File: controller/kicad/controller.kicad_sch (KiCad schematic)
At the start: 22 parts, among them J1 pcie_98, U1 ESD5344D, U10 ESD5344D, U11 WeAct_STM32H750_Module, U12 ESD5344D, U13 ESD5344D, U14 ESD5344D, U15 ESD5344D, U16 ESD5344D, U17 ESD5344D, U18 ESD5344D, U19 ESD5344D, U2 ESD5344D, U20 ESD5344D, U21 ESD5344D, U3 ESD5344D, U4 ESD5344D, U5 ESD5344D, U6 ESD5344D, U7 ESD5344D, U8 ESD5344D, U9 ESD5344D

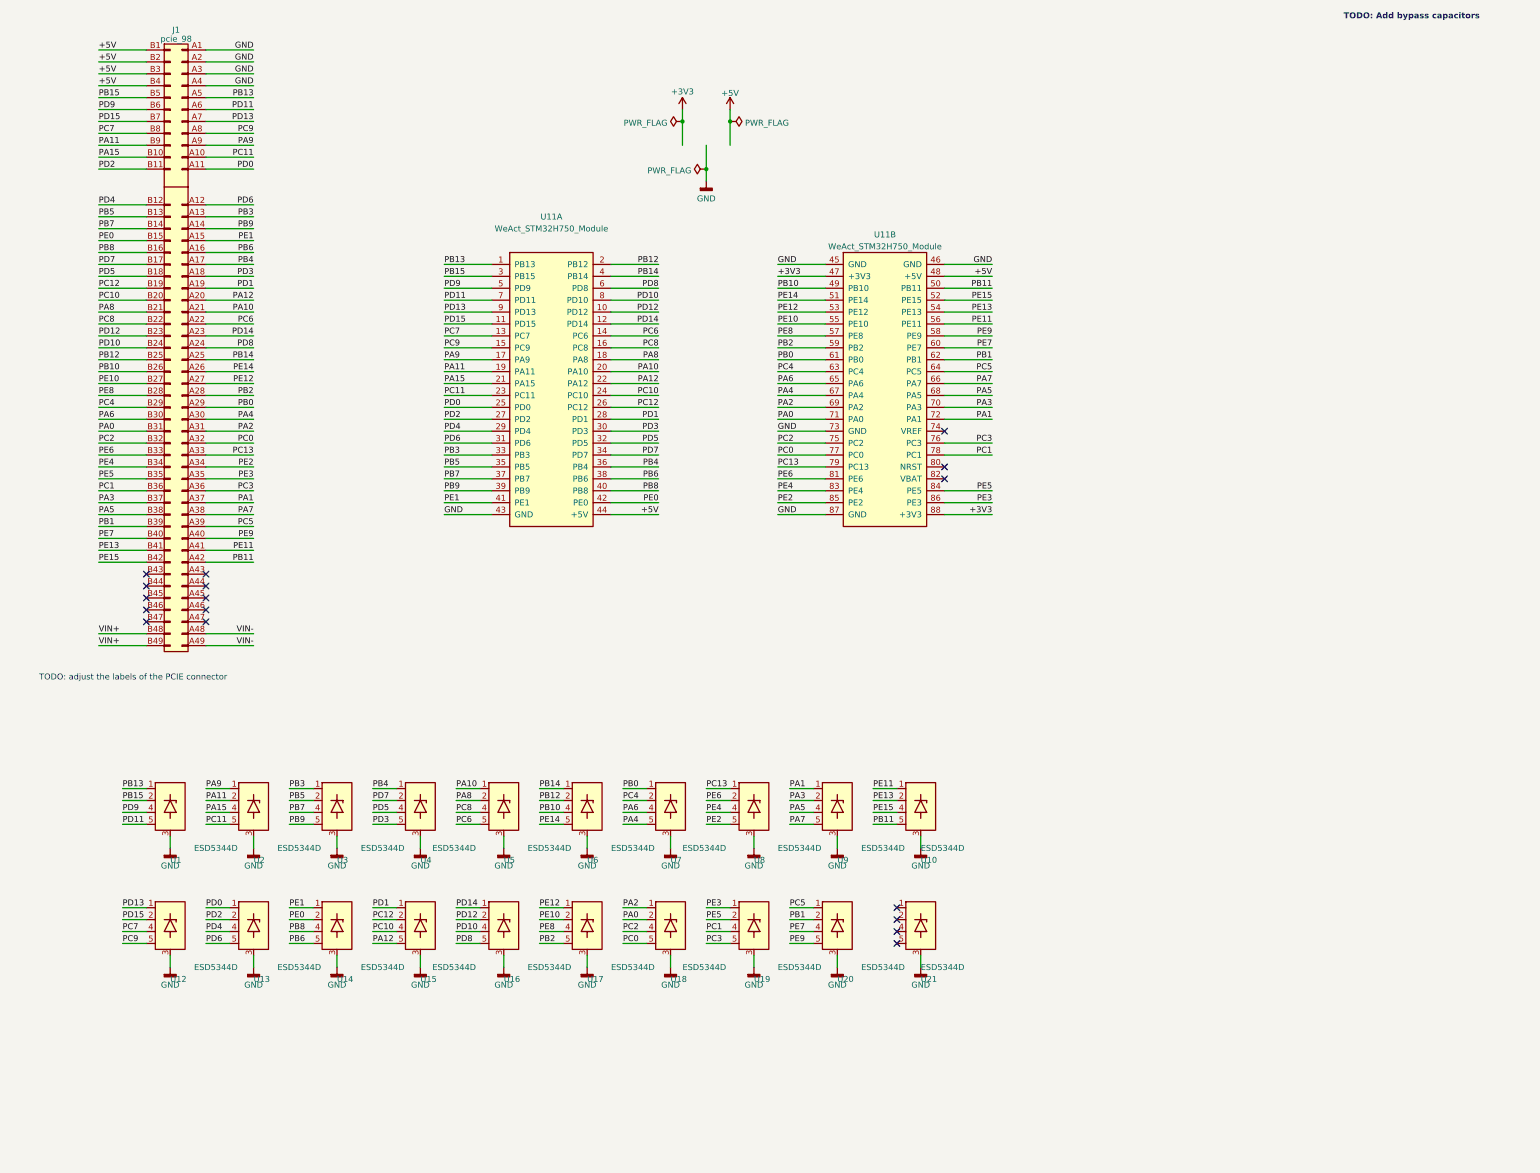
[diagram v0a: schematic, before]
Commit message: Controller board passes ERC and DRC. Needs more cleanup.
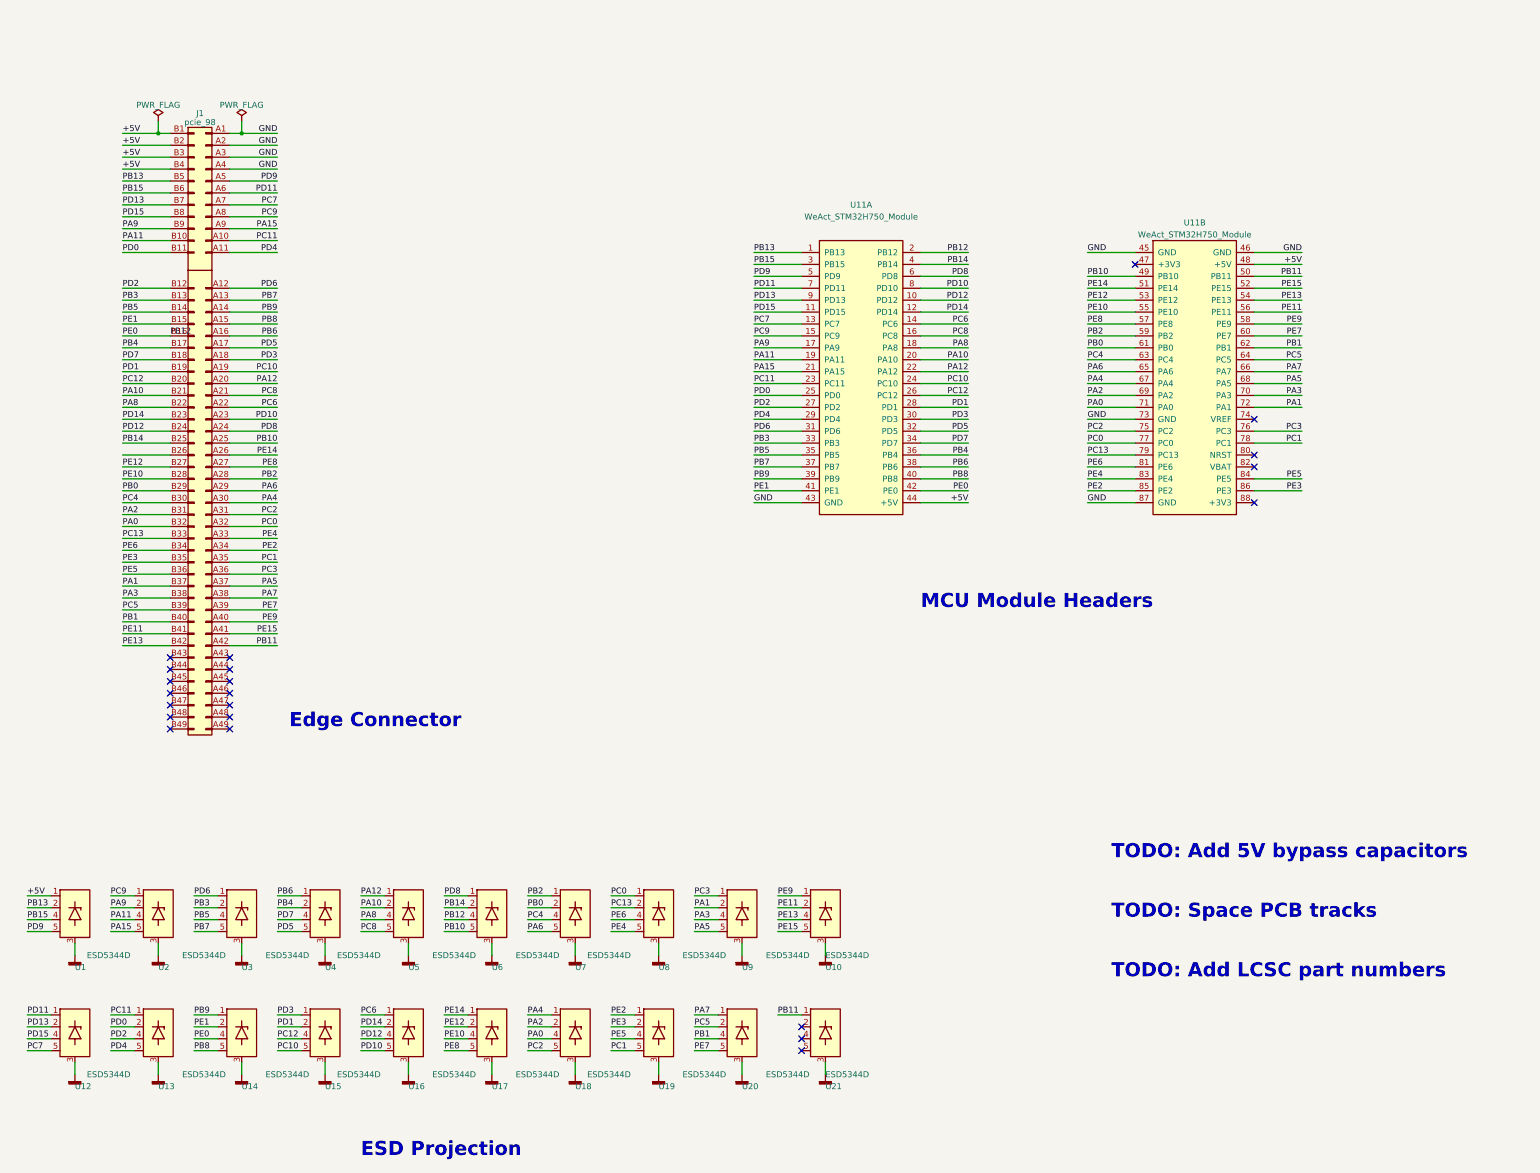
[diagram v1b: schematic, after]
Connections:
- net +5V: now also U1.1 (D1)
- net PA0: now also J1.B32 (Pin_b32), U18.4 (D3); no longer J1.B31 (Pin_b31), U18.2 (D2)
- net PA1: now also J1.B37 (Pin_b37), U9.2 (D2); no longer J1.A37 (Pin_a37), U9.1 (D1)
- net PA10: now also J1.B21 (Pin_b21), U5.2 (D2); no longer J1.A21 (Pin_a21), U5.1 (D1)
- net PA11: now also J1.B10 (Pin_b10), U2.4 (D3); no longer J1.B9 (Pin_b9), U2.2 (D2)
- net PA12: now also U5.1 (D1); no longer U15.5 (D4)
- net PA15: now also J1.A9 (Pin_a9), U2.5 (D4); no longer J1.B10 (Pin_b10), U2.4 (D3)
- net PA2: now also J1.B31 (Pin_b31), U18.2 (D2); no longer J1.A31 (Pin_a31), U18.1 (D1)
- net PA3: now also J1.B38 (Pin_b38), U9.4 (D3); no longer J1.B37 (Pin_b37), U9.2 (D2)
- net PA4: now also U18.1 (D1); no longer U7.5 (D4)
- net PA5: now also J1.A37 (Pin_a37), U9.5 (D4); no longer J1.B38 (Pin_b38), U9.4 (D3)
- net PA6: now also J1.A29 (Pin_a29), U7.5 (D4); no longer J1.B30 (Pin_b30), U7.4 (D3)
- net PA7: now also U20.1 (D1); no longer U9.5 (D4)
- net PA8: now also J1.B22 (Pin_b22), U5.4 (D3); no longer J1.B21 (Pin_b21), U5.2 (D2)
- net PA9: now also J1.B9 (Pin_b9), U2.2 (D2); no longer J1.A9 (Pin_a9), U2.1 (D1)
- net PB0: now also J1.B29 (Pin_b29), U7.2 (D2); no longer J1.A29 (Pin_a29), U7.1 (D1)
- net PB1: now also J1.B40 (Pin_b40), U20.4 (D3); no longer J1.B39 (Pin_b39), U20.2 (D2)
- net PB10: now also J1.A25 (Pin_a25), U6.5 (D4); no longer J1.B26 (Pin_b26), U6.4 (D3)
- net PB11: now also U21.1 (D1); no longer U10.5 (D4)
- net PB12: now also J1.B16 (Pin_b16), U11.42 (PE0), U14.4 (D3), U6.4 (D3); no longer J1.B25 (Pin_b25), U6.2 (D2)
- net PB13: now also J1.B5 (Pin_b5), U1.2 (D2); no longer J1.A5 (Pin_a5), U1.1 (D1)
- net PB14: now also J1.B25 (Pin_b25), U6.2 (D2); no longer J1.A25 (Pin_a25), U6.1 (D1)
- net PB15: now also J1.B6 (Pin_b6), U1.4 (D3); no longer J1.B5 (Pin_b5), U1.2 (D2)
- net PB2: now also U7.1 (D1); no longer U17.5 (D4)
- net PB3: now also J1.B13 (Pin_b13), U3.2 (D2); no longer J1.A13 (Pin_a13), U3.1 (D1)
- net PB4: now also J1.B17 (Pin_b17), U4.2 (D2); no longer J1.A17 (Pin_a17), U4.1 (D1)
- net PB5: now also J1.B14 (Pin_b14), U3.4 (D3); no longer J1.B13 (Pin_b13), U3.2 (D2)
- net PB6: now also U4.1 (D1); no longer U14.5 (D4)
- net PB7: now also J1.A13 (Pin_a13), U3.5 (D4); no longer J1.B14 (Pin_b14), U3.4 (D3)
- net PB8: now also J1.A15 (Pin_a15), U14.5 (D4); no longer J1.B16 (Pin_b16), U14.4 (D3)
- net PB9: now also U14.1 (D1); no longer U3.5 (D4)
- net PC0: now also U8.1 (D1); no longer U18.5 (D4)
- net PC1: now also J1.A35 (Pin_a35), U19.5 (D4); no longer J1.B36 (Pin_b36), U19.4 (D3)
- net PC10: now also J1.A19 (Pin_a19), U15.5 (D4); no longer J1.B20 (Pin_b20), U15.4 (D3)
- net PC11: now also U13.1 (D1); no longer U2.5 (D4)
- net PC12: now also J1.B20 (Pin_b20), U15.4 (D3); no longer J1.B19 (Pin_b19), U15.2 (D2)
- net PC13: now also J1.B33 (Pin_b33), U8.2 (D2); no longer J1.A33 (Pin_a33), U8.1 (D1)
- net PC2: now also J1.A31 (Pin_a31), U18.5 (D4); no longer J1.B32 (Pin_b32), U18.4 (D3)
- net PC3: now also U9.1 (D1); no longer U19.5 (D4)
- net PC4: now also J1.B30 (Pin_b30), U7.4 (D3); no longer J1.B29 (Pin_b29), U7.2 (D2)
- net PC5: now also J1.B39 (Pin_b39), U20.2 (D2); no longer J1.A39 (Pin_a39), U20.1 (D1)
- net PC6: now also U16.1 (D1); no longer U5.5 (D4)
- net PC7: now also J1.A7 (Pin_a7), U12.5 (D4); no longer J1.B8 (Pin_b8), U12.4 (D3)
- net PC8: now also J1.A21 (Pin_a21), U5.5 (D4); no longer J1.B22 (Pin_b22), U5.4 (D3)
- net PC9: now also U2.1 (D1); no longer U12.5 (D4)
- net PD0: now also J1.B11 (Pin_b11), U13.2 (D2); no longer J1.A11 (Pin_A11), U13.1 (D1)
- net PD1: now also J1.B19 (Pin_b19), U15.2 (D2); no longer J1.A19 (Pin_a19), U15.1 (D1)
- net PD10: now also J1.A23 (Pin_a23), U16.5 (D4); no longer J1.B24 (Pin_b24), U16.4 (D3)
- net PD11: now also U12.1 (D1); no longer U1.5 (D4)
- net PD12: now also J1.B24 (Pin_b24), U16.4 (D3); no longer J1.B23 (Pin_b23), U16.2 (D2)
- net PD13: now also J1.B7 (Pin_b7), U12.2 (D2); no longer J1.A7 (Pin_a7), U12.1 (D1)
- net PD14: now also J1.B23 (Pin_b23), U16.2 (D2); no longer J1.A23 (Pin_a23), U16.1 (D1)
- net PD15: now also J1.B8 (Pin_b8), U12.4 (D3); no longer J1.B7 (Pin_b7), U12.2 (D2)
- net PD2: now also J1.B12 (Pin_b12), U13.4 (D3); no longer J1.B11 (Pin_b11), U13.2 (D2)
- net PD3: now also U15.1 (D1); no longer U4.5 (D4)
- net PD4: now also J1.A11 (Pin_A11), U13.5 (D4); no longer J1.B12 (Pin_b12), U13.4 (D3)
- net PD5: now also J1.A17 (Pin_a17), U4.5 (D4); no longer J1.B18 (Pin_b18), U4.4 (D3)
- net PD6: now also U3.1 (D1); no longer U13.5 (D4)
- net PD7: now also J1.B18 (Pin_b18), U4.4 (D3); no longer J1.B17 (Pin_b17), U4.2 (D2)
- net PD8: now also U6.1 (D1); no longer U16.5 (D4)
- net PD9: now also J1.A5 (Pin_a5), U1.5 (D4); no longer J1.B6 (Pin_b6), U1.4 (D3)
- net PE1: now also J1.B15 (Pin_b15), U14.2 (D2); no longer J1.A15 (Pin_a15), U14.1 (D1)
- net PE10: now also J1.B28 (Pin_b28), U17.4 (D3); no longer J1.B27 (Pin_b27), U17.2 (D2)
- net PE11: now also J1.B41 (Pin_b41), U10.2 (D2); no longer J1.A41 (Pin_a41), U10.1 (D1)
- net PE12: now also J1.B27 (Pin_b27), U17.2 (D2); no longer J1.A27 (Pin_a27), U17.1 (D1)
- net PE13: now also J1.B42 (Pin_b42), U10.4 (D3); no longer J1.B41 (Pin_b41), U10.2 (D2)
- net PE14: now also U17.1 (D1); no longer U6.5 (D4)
- net PE15: now also J1.A41 (Pin_a41), U10.5 (D4); no longer J1.B42 (Pin_b42), U10.4 (D3)
- net PE2: now also U19.1 (D1); no longer U8.5 (D4)
- net PE3: now also J1.B35 (Pin_b35), U19.2 (D2); no longer J1.A35 (Pin_a35), U19.1 (D1)
- net PE4: now also J1.A33 (Pin_a33), U8.5 (D4); no longer J1.B34 (Pin_b34), U8.4 (D3)
- net PE5: now also J1.B36 (Pin_b36), U19.4 (D3); no longer J1.B35 (Pin_b35), U19.2 (D2)
- net PE6: now also J1.B34 (Pin_b34), U8.4 (D3); no longer J1.B33 (Pin_b33), U8.2 (D2)
- net PE7: now also J1.A39 (Pin_a39), U20.5 (D4); no longer J1.B40 (Pin_b40), U20.4 (D3)
- net PE8: now also J1.A27 (Pin_a27), U17.5 (D4); no longer J1.B28 (Pin_b28), U17.4 (D3)
- net PE9: now also U10.1 (D1); no longer U20.5 (D4)
- net +3V3: no longer names the net of U11.47 (+3V3)
- net +3V3: no longer U11.88 (+3V3)
- removed net PE0: J1.B15 (Pin_b15), U11.42 (PE0), U14.2 (D2)
- net VIN+: no longer names the net of J1.B48 (Pin_b48)
- net VIN+: no longer J1.B49 (Pin_b49)
- net VIN-: no longer names the net of J1.A48 (Pin_a48)
- net VIN-: no longer J1.A49 (Pin_a49)
- no-connect marks 17 -> 22
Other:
- note added: "ESD Projection"
- note added: "Edge Connector"
- note added: "MCU Module Headers"
- note added: "TODO: Add 5V bypass capacitors"
- note added: "TODO: Add LCSC part numbers"
- note added: "TODO: Space PCB tracks"
- note removed: "TODO: Add bypass capacitors"
- note removed: "TODO: adjust the labels of the PCIE connector"
- moved on the sheet: J1, U1, U10, U11A, U11B, U12, U13, U14, U15, U16, U17, U18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

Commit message: Added to the controller boared 5V power arbitration.
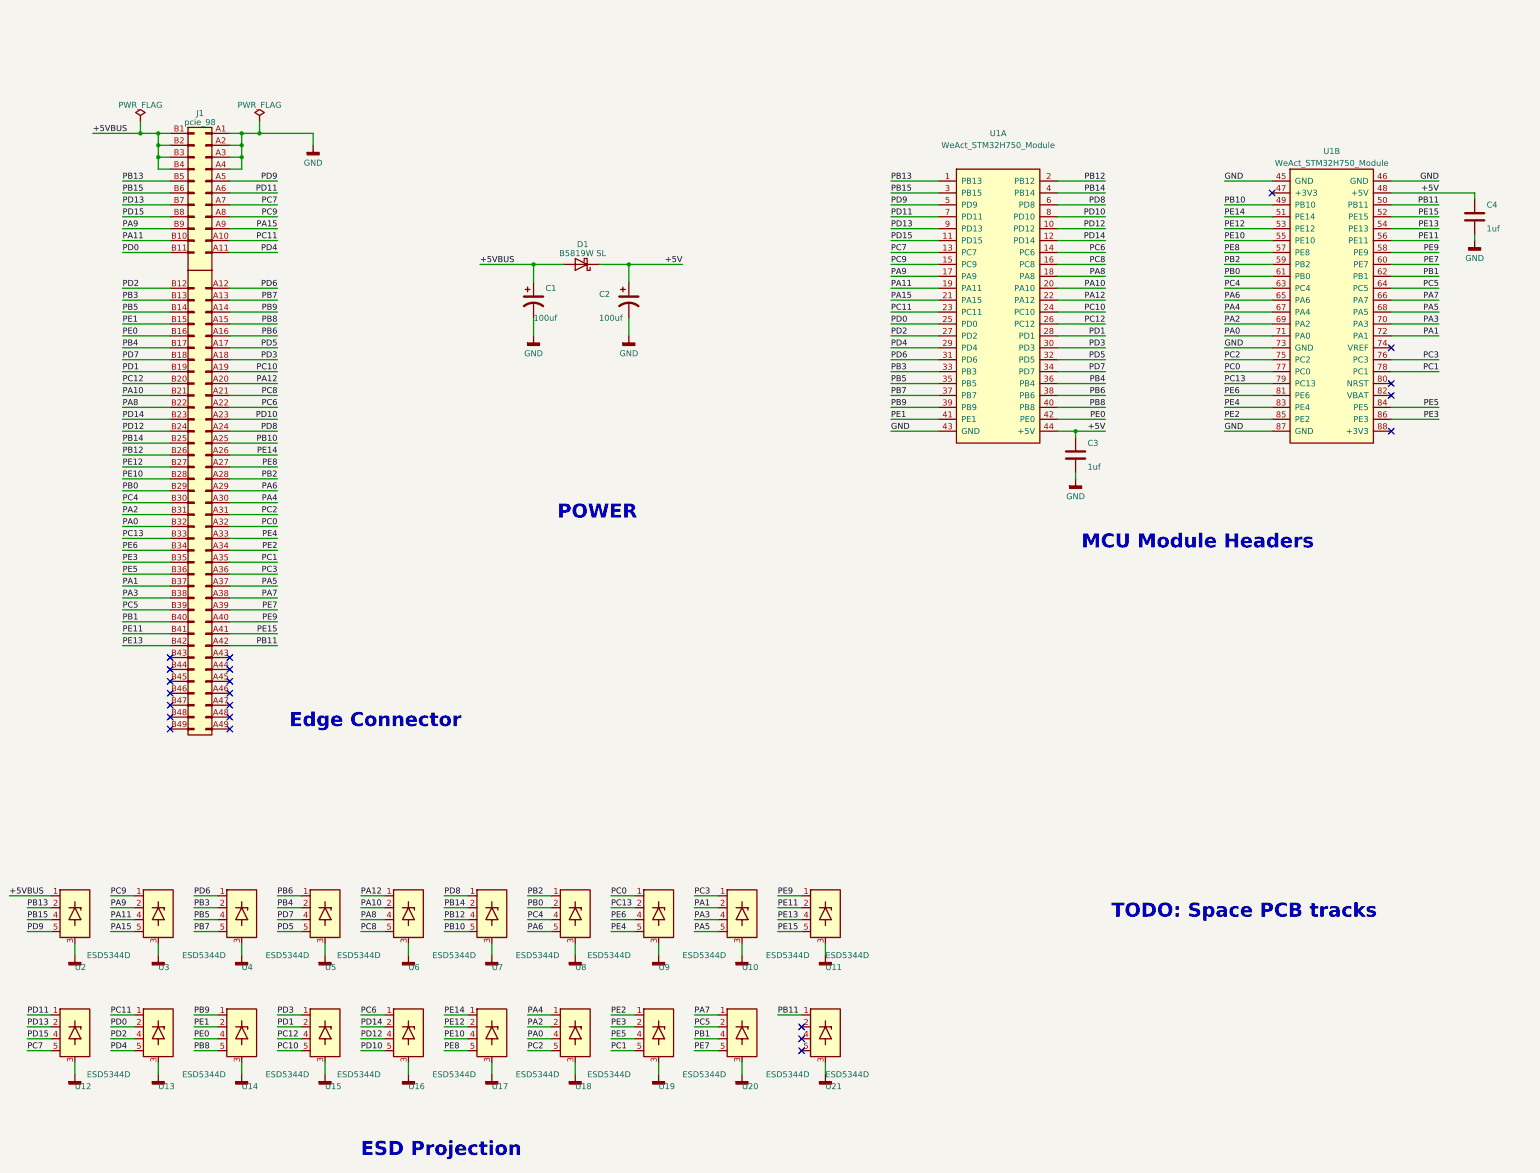
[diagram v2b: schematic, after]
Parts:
- added C1, C2: 100uf, Capacitor_SMD:CP_Elec_5x5.4, symbol Device:C_Polarized_US
- added C3, C4: 1uf, Capacitor_SMD:C_0201_0603Metric, symbol Device:C
- added D1: B5819W SL, Diode_SMD:D_SOD-123, symbol Device:D_Schottky
- J1: LCSC (none) -> DNP; now left out of the parts list
- U10: renamed from U9; LCSC (none) -> C2841840
- U11: renamed from U10; LCSC (none) -> C2841840
- U12, U13, U14, U15, U16, U17, U18, U19, U20, U21: LCSC (none) -> C2841840
- U2: renamed from U1; LCSC (none) -> C2841840
- U3: renamed from U2; LCSC (none) -> C2841840
- U4: renamed from U3; LCSC (none) -> C2841840
- U5: renamed from U4; LCSC (none) -> C2841840
- U6: renamed from U5; LCSC (none) -> C2841840
- U7: renamed from U6; LCSC (none) -> C2841840
- U8: renamed from U7; LCSC (none) -> C2841840
- U9: renamed from U8; LCSC (none) -> C2841840
- renumbered U11 to U1
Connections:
- net +5V: now also C2.1, C3.1, C4.1, D1.1 (K); no longer J1.B1 (Pin_b1), J1.B2 (Pin_b2), J1.B3 (Pin_b3), J1.B4 (Pin_b4), U2.1 (D1)
- net GND: now also C1.2, C2.2, C3.2, C4.2
- net PB12: now also J1.B26 (Pin_b26); no longer J1.B16 (Pin_b16), U1.42 (PE0), U14.4 (D3)
- new net +5VBUS: C1.1, D1.2 (A), J1.B1 (Pin_b1), J1.B2 (Pin_b2), J1.B3 (Pin_b3), J1.B4 (Pin_b4), U2.1 (D1)
- new net PE0: J1.B16 (Pin_b16), U1.42 (PE0), U14.4 (D3)
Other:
- note added: "POWER"
- note removed: "TODO: Add 5V bypass capacitors"
- note removed: "TODO: Add LCSC part numbers"
- moved on the sheet: U1A, U1B
